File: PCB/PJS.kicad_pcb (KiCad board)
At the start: 2 copper layers, 127 x 127 mm, 40 parts, among them J1 HFW8R-1STE1H1LF_FFC, J10 SM02B-PASS-TBT_SwitchConnector, J2 SM02B-PASS-TBT_Connector, J3 SM02B-PASS-TBT_Connector, J4 SM02B-PASS-TBT_Connector, J5 SM02B-PASS-TBT_Connector, J6 SM02B-PASS-TBT_SwitchConnector, J7 SM02B-PASS-TBT_SwitchConnector, J8 SM02B-PASS-TBT_SwitchConnector, J9 SM02B-PASS-TBT_SwitchConnector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

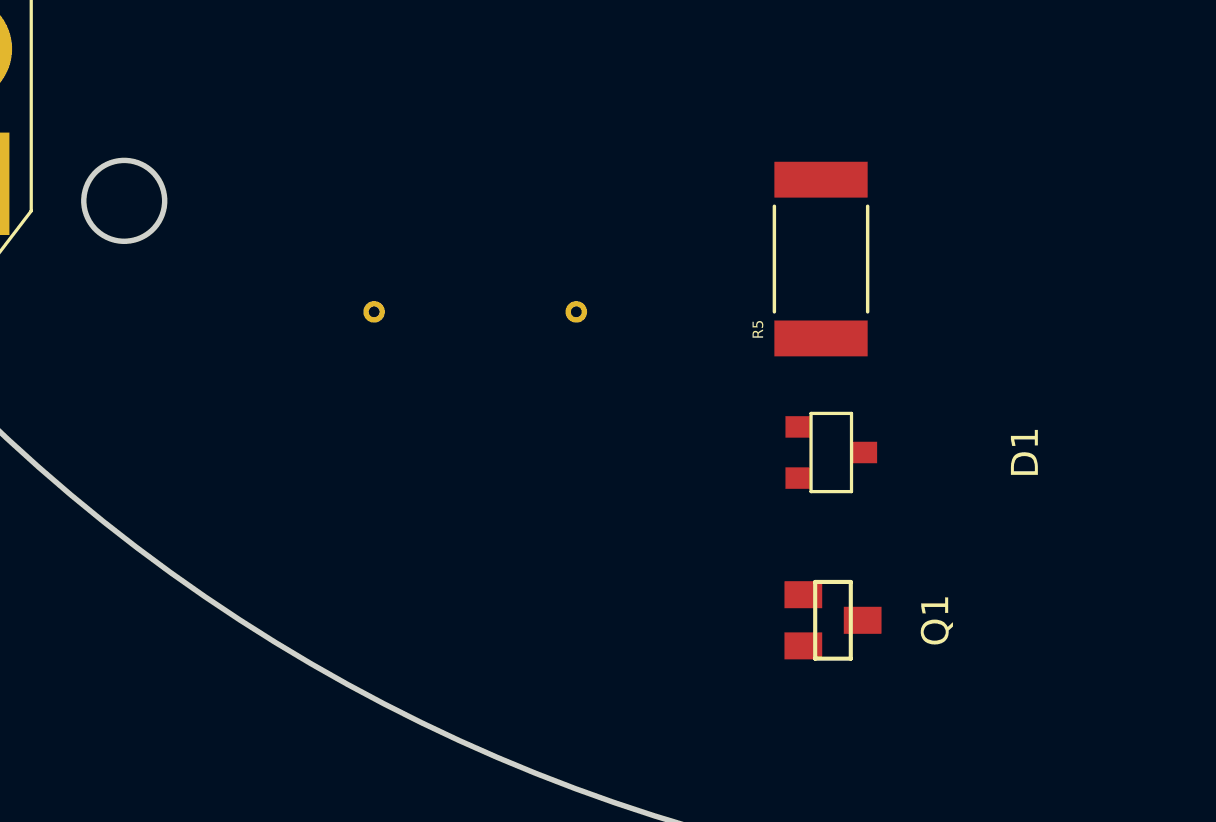
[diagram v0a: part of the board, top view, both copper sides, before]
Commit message: Updated DRV8871 footprint
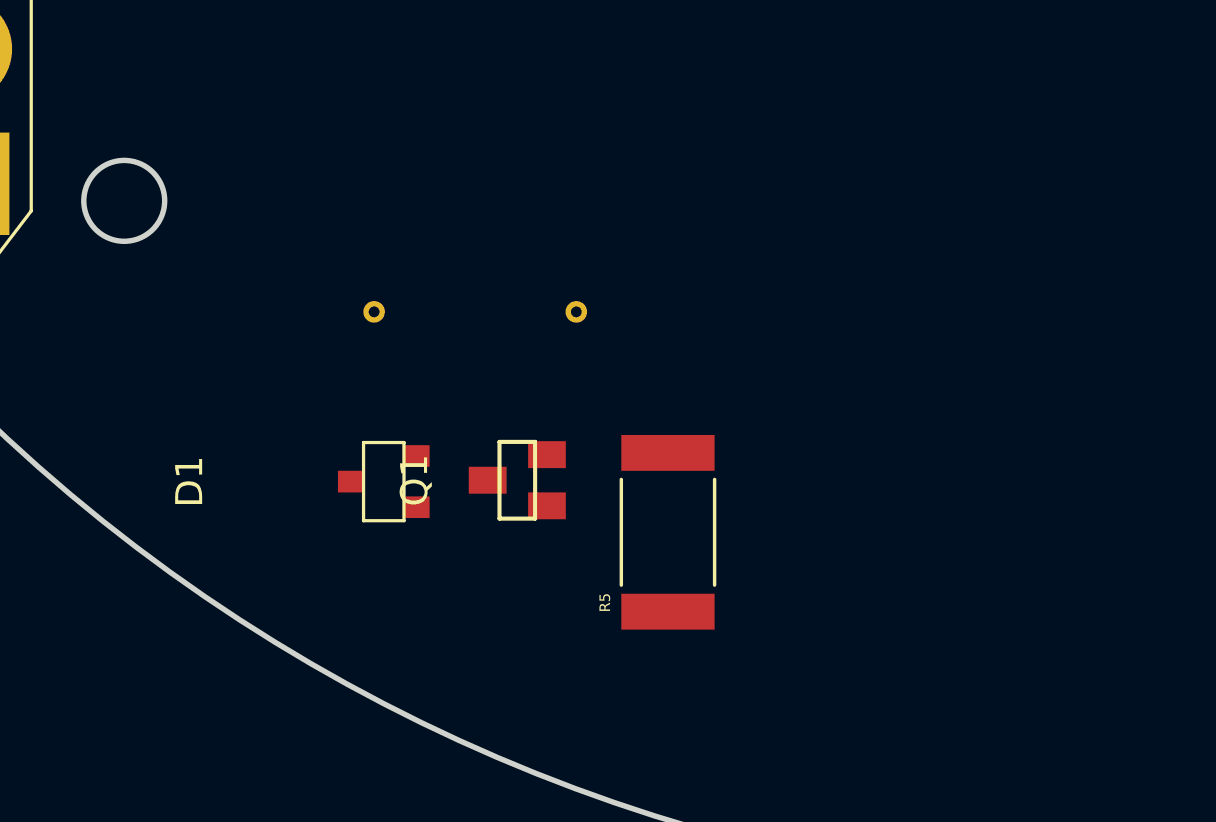
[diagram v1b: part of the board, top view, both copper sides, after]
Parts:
- moved D1 16.6 mm to (101.7, 146.9), turned to 90 degrees
- moved Q1 12.8 mm to (106.7, 146.9), turned to 90 degrees
- moved R5 11.6 mm to (112.2, 148.8)
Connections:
- J3 pad 1: /Link_DriverOutA -> /Link_DriverOUT1
- J3 pad 2: /Link_DriverOutB -> /Link_DriverOUT2
- J4 pad 2: /LockA_DriverOut2 -> /LockA_DriverOUT2
- K1 pad 1: Net-(D1-Pad2) -> +5V
- K1 pad 8: +5V -> Net-(D1-Pad2)
